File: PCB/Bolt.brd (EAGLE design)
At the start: 160 x 100 mm, 11 parts, among them IC1 D36V28FX, U1 MPU-9250, U2 ESP32-WROOM-32D, U3 TB6612FNG(O,C,8,EL

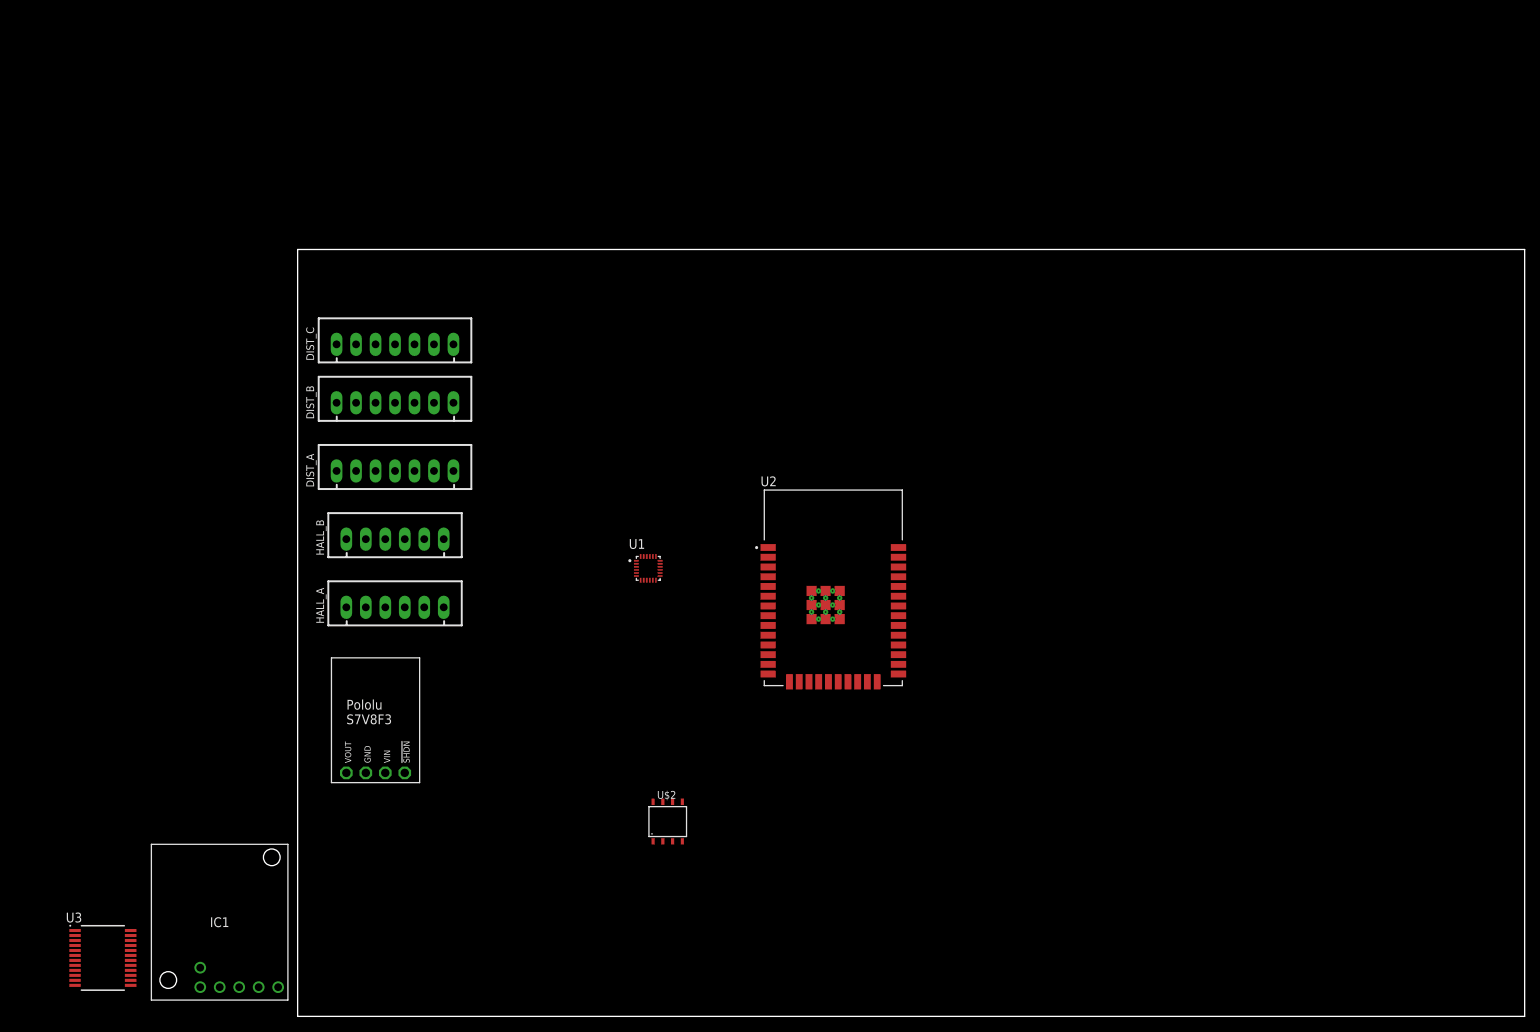
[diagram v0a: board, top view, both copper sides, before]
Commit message: Added UART-USB converter
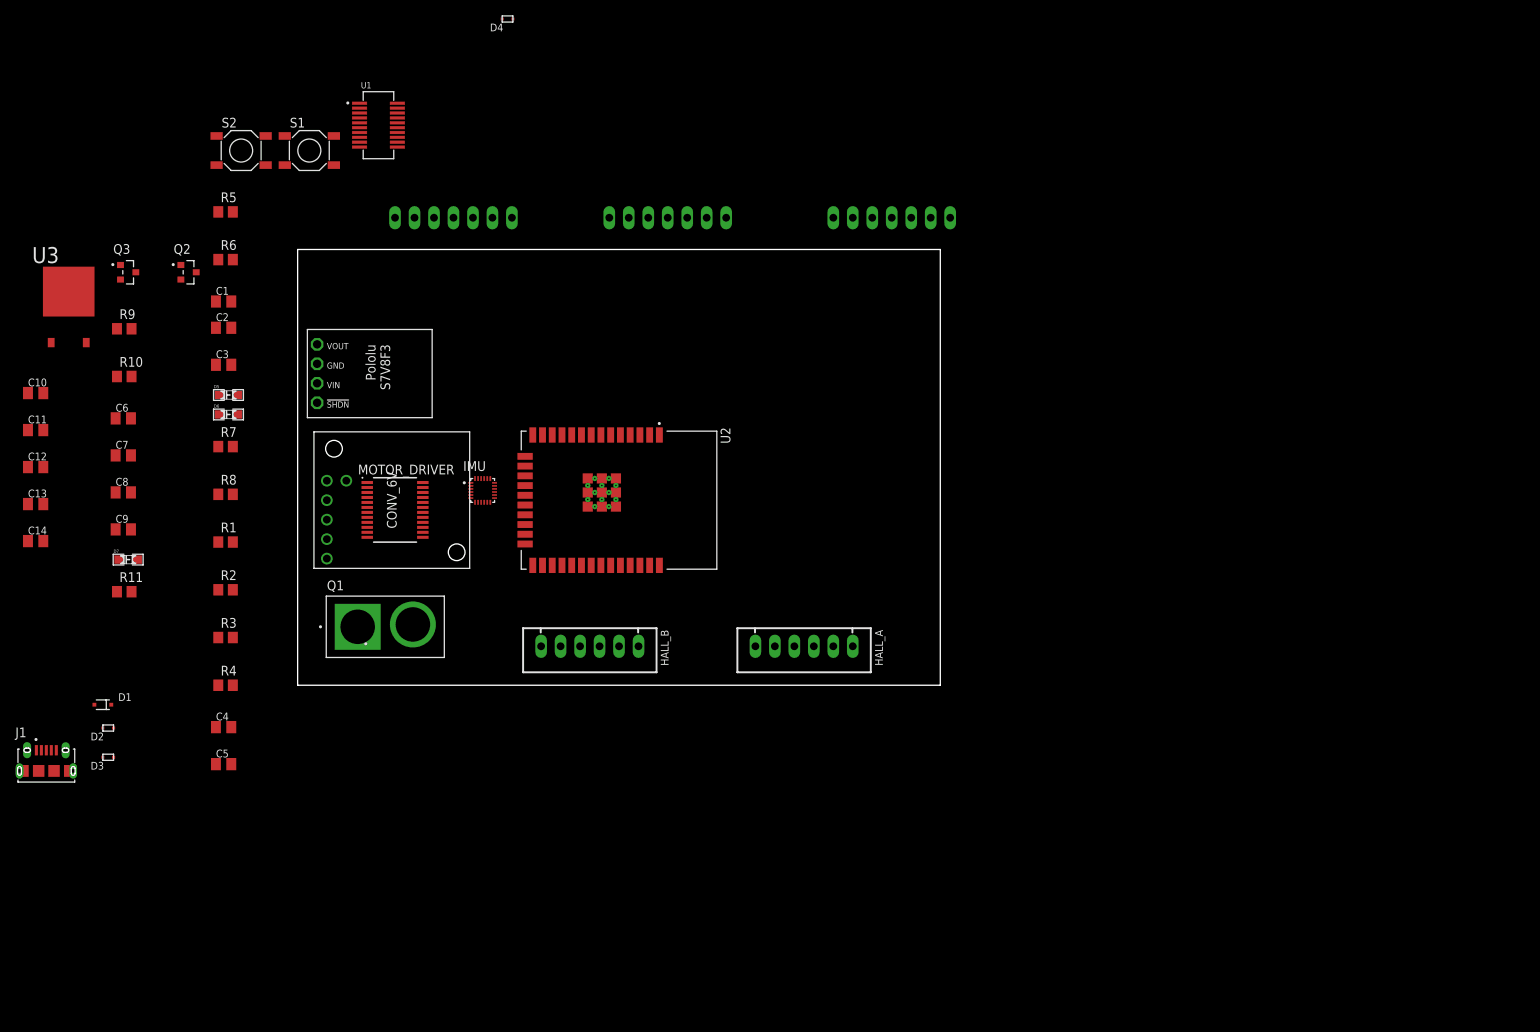
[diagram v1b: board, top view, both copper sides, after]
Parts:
- removed IC1: D36V28FX, D36V28FX:D36V28FX
- removed U$1: S7V8F3, Pololu_S7V8F3:S7V8F3
- removed U$2: TP4056, TP4056:SOT23-8
- added C1, C2: 47pF, rcl:C0805K
- added C10, C13: 1uF, rcl:C0805K
- added C11, C6: 10uF, rcl:C0805K
- added C12, C3, C7, C8: 0.1uF, rcl:C0805K
- added C14: 47uF, rcl:C0805K
- added C4, C5: 1nF, rcl:C0805K
- added C9: 22uF, rcl:C0805K
- added CONV_3V3: S7V8F3, Pololu_S7V8F3:S7V8F3
- added CONV_6V: D36V28FX, D36V28FX:D36V28FX
- added D1: BAT760,115, BAT760_115:SOD323(F)
- added D2, D3, D4: ESD5B5.0ST1G, ESD5B5.0ST1G:SOD-523
- added D5, D6: (no value), leds:0805.LED
- added D7: 3.3V, leds:0805.LED
- added IMU: MPU-9250, MPU-9250:QFN40P300X300X105-24N
- added J1: 10118194-0001LF, 10118194-0001LF:AMPHENOL_10118194-0001LF
- added MOTOR_DRIVER: TB6612FNG(O,C,8,EL, TB6612FNG_O_C_8_EL:SOP65P760X160-24N
- added Q1: XT60_YELLOW, XT60_YELLOW:AMASS_XT60PB-M
- added Q2, Q3: MMSS8050-H-TP, MMSS8050-H-TP:TRANS_MMSS8050-H-TP
- added R1, R2: 220R, rcl:R0805
- added R10, R3, R4, R7, R8, R9: 10K, rcl:R0805
- added R11: 1K, rcl:R0805
- added R5, R6: 27R, rcl:R0805
- added S1, S2: PTS525SM08, pts525_20:SM08
- U1: value MPU-9250 -> FT231XS-R; device MPU-9250:QFN40P300X300X105-24N -> FT231XS-R:SOP63P599X175-20N
- U3: value TB6612FNG(O,C,8,EL -> LM1117DT-3.3/NOPB; device TB6612FNG_O_C_8_EL:SOP65P760X160-24N -> LM1117DT-3.3_NOPB:TO228P970X238-3N
- moved U3 86.9 mm to (-29.8, 94.4)
- moved DIST_B 69.1 mm to (77.5, 104.1), flipped to the bottom
- moved U1 67.7 mm to (10.5, 116.2)
- moved HALL_A 53.6 mm to (66.0, 48.3), turned to 180 degrees
- moved DIST_A 48.5 mm to (48.3, 104.1), flipped to the bottom
- moved U2 30.2 mm to (41.9, 67.3), turned to 270 degrees
- moved HALL_B 29.0 mm to (38.1, 48.3), turned to 180 degrees
- moved DIST_C 18.2 mm to (20.3, 104.1), flipped to the bottom
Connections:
- net N$73 renamed CTS
- removed net VM1: U3.24
- removed net VM2: U3.13
- removed net VM3: U3.14
- new net 6V: CONV_6V.6
- new net DTR: Q2.2, R9.2, U1.1
- new net EN: C5.1, Q3.3, R1.1, R4.2, U2.3
- new net EXT_5V: C10.1, C11.1, D1.1, U1.15, U3.3
- new net GND: C1.2, C10.2, C11.2, C12.2, C13.2, C14.2, C2.2, C3.2, C4.2, C5.2, C6.2, C7.2, C8.2, C9.2, CONV_3V3.GND, CONV_6V.4, CONV_6V.5, D2.P$2, D3.P$2, D4.P$2, J1.1, J1.S1, J1.S2, J1.S3, J1.S4, J1.S5, J1.S6, Q1.2, R11.1, S1.3, S2.3, U1.16, U1.6, U2.1, U2.15, U2.38, U2.39_1, U2.39_10, U2.39_11, U2.39_12, U2.39_13, U2.39_14, U2.39_15, U2.39_16, U2.39_17, U2.39_18, U2.39_19, U2.39_2, U2.39_20, U2.39_21, U2.39_3, U2.39_4, U2.39_5, U2.39_6, U2.39_7, U2.39_8, U2.39_9, U3.1
- new net IO0: C4.1, Q2.3, R2.1, R3.2, U2.25
- new net N$100: MOTOR_DRIVER.2
- new net N$101: MOTOR_DRIVER.5
- new net N$102: MOTOR_DRIVER.6
- new net N$103: MOTOR_DRIVER.1
- new net N$104: MOTOR_DRIVER.24
- new net N$105: MOTOR_DRIVER.13
- new net N$106: MOTOR_DRIVER.14
- new net N$107: MOTOR_DRIVER.20
- new net N$110: CONV_3V3.!SHDN
- new net N$112: CONV_6V.1
- new net N$113: CONV_6V.2
- new net N$122: U1.5
- new net N$124: Q3.1, R9.1
- new net N$126: D5.P$2, U1.17
- new net N$127: D6.P$2, U1.10
- new net N$129: D6.P$1, R8.2
- new net N$73: IMU.9
- new net N$74: IMU.7
- new net N$80: IMU.8
- new net N$84: MOTOR_DRIVER.19
- new net N$85: MOTOR_DRIVER.23
- new net N$86: MOTOR_DRIVER.15
- new net N$87: MOTOR_DRIVER.21
- new net N$88: MOTOR_DRIVER.22
- new net N$89: MOTOR_DRIVER.17
- new net N$90: MOTOR_DRIVER.16
- new net N$91: MOTOR_DRIVER.4
- new net N$92: MOTOR_DRIVER.3
- new net N$93: MOTOR_DRIVER.18
- new net N$94: MOTOR_DRIVER.9
- new net N$95: MOTOR_DRIVER.10
- new net N$96: MOTOR_DRIVER.12
- new net N$97: MOTOR_DRIVER.7
- new net N$98: MOTOR_DRIVER.8
- new net N$99: MOTOR_DRIVER.11
- new net RTS: Q2.1, Q3.2, R10.1, R10.2, U1.2
- new net RXD0: U1.20, U2.34
- new net TXD0: U1.4, U2.35
- new net USB_5V: C6.1, C7.1, D1.2, D4.P$1, J1.5
- new net USB_DM: C2.1, D2.P$1, J1.4, R6.1
- new net USB_DP: C1.1, D3.P$1, J1.3, R5.1
- new net V_BAT: CONV_3V3.VIN, CONV_6V.3, Q1.1
- net N$28: now also D7.P$2, R11.2; no longer U2.2
- net N$35: now also D5.P$1, R7.2; no longer U2.25
- net N$55: now also R5.2, U1.11; no longer U2.3
- net N$56: now also R6.2, U1.12; no longer U2.1, U2.15, U2.38, U2.39_1, U2.39_10, U2.39_11, U2.39_12, U2.39_13, U2.39_14, U2.39_15, U2.39_16, U2.39_17, U2.39_18, U2.39_19, U2.39_2, U2.39_20, U2.39_21, U2.39_3, U2.39_4, U2.39_5, U2.39_6, U2.39_7, U2.39_8, U2.39_9
- net N$61: now also R2.2, S1.1; no longer U2.35
- net N$62: now also R1.2, S2.1; no longer U2.34
- net N$69: now also IMU.11; no longer U1.11
- net N$70: now also IMU.22; no longer U1.22
- net N$71: now also IMU.23; no longer U1.23
- net N$72: now also IMU.24; no longer U1.24
- net N$75: now also IMU.21; no longer U1.21
- net N$76: now also IMU.1; no longer U1.1
- net N$77: now also IMU.19; no longer U1.19
- net N$78: now also IMU.20; no longer U1.20
- net N$79: now also IMU.13; no longer U1.13
- net N$81: now also IMU.12; no longer U1.12
- net N$82: now also IMU.10; no longer U1.10
- net N$83: now also IMU.18; no longer U1.18
- net VCC: now also C12.1, C13.1, C14.1, C3.1, C8.1, C9.1, CONV_3V3.VOUT, D7.P$1, R3.1, R4.1, R7.1, R8.1, U1.13, U1.14, U1.3, U2.2, U3.2; no longer U3.20
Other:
- board size 160 x 100 mm -> 83.8 x 56.8 mm

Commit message: Schematic completed
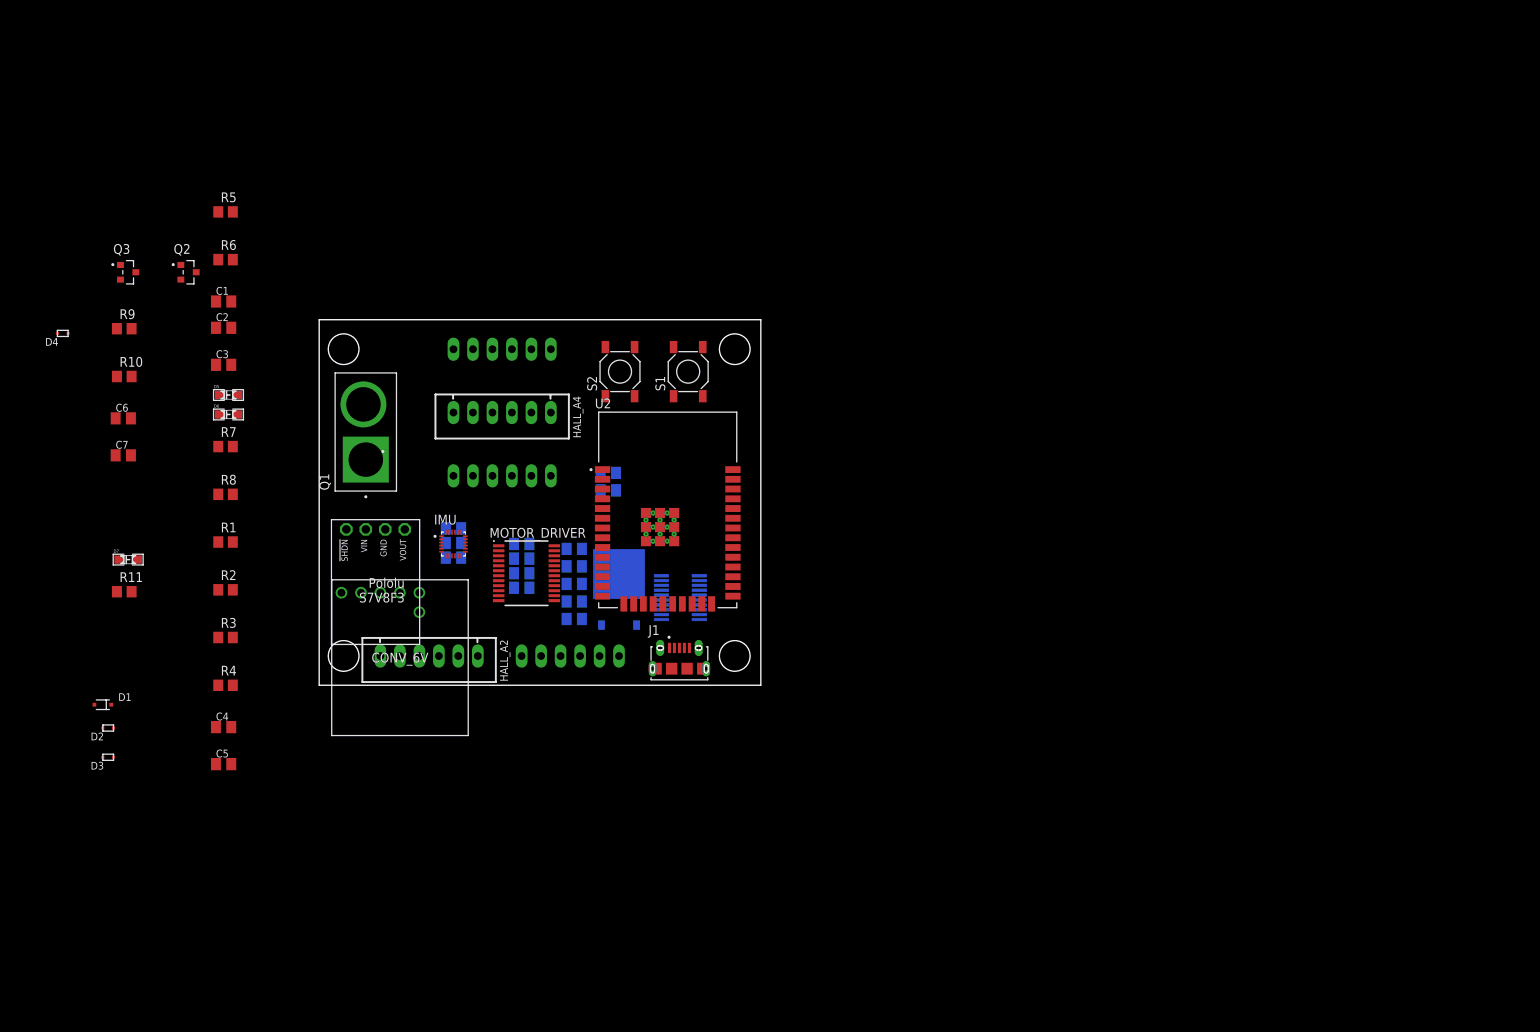
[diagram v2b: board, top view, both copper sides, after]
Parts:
- removed DIST_A, DIST_B, DIST_C: JST-XH-07-PIN-LONG-PAD, Rembrandt Electronics - JST XH Connectors v1-0:JST-XH-07-PACKAGE-LONG-PAD
- removed HALL_B: JST-XH-06-PIN-LONG-PAD, Rembrandt Electronics - JST XH Connectors v1-0:JST-XH-06-PACKAGE-LONG-PAD
- added C15, C17, C19, C20: 0.1uF, rcl:C0805K
- added C16, C18: 10uF, rcl:C0805K
- added C21: 10nF, rcl:C0805K
- added HALL_A1, HALL_A2, HALL_A3, HALL_A4: JST-XH-06-PIN-LONG-PAD, Rembrandt Electronics - JST XH Connectors v1-0:JST-XH-06-PACKAGE-LONG-PAD
- moved J1 83.6 mm to (49.8, 45.3)
- moved U3 80.7 mm to (41.9, 57.5), flipped to the bottom
- moved C10 73.1 mm to (36.1, 61.0), flipped to the bottom
- moved U1 73.1 mm to (49.9, 54.6), flipped to the bottom, turned to 180 degrees
- moved C11 72.4 mm to (36.1, 58.7), flipped to the bottom
- moved C12 71.9 mm to (36.1, 56.4), flipped to the bottom
- moved C13 71.4 mm to (36.1, 54.1), flipped to the bottom
- moved D4 71.0 mm to (-31.3, 89.6)
- moved C14 71.0 mm to (36.1, 51.8), flipped to the bottom
- moved C9 63.4 mm to (40.5, 68.6), flipped to the bottom
- moved C8 63.3 mm to (40.5, 70.9), flipped to the bottom
- moved S1 57.2 mm to (50.9, 84.1), turned to 90 degrees
- moved S2 57.2 mm to (42.0, 84.1), turned to 90 degrees
- moved HALL_A 30.5 mm to (35.6, 47.0), flipped to the bottom
- moved Q1 25.5 mm to (8.89, 76.2), turned to 90 degrees
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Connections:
- net N$25 renamed HALL_1_A
- net N$69 renamed IMU_FSYNC
- net N$70 renamed IMU_CS
- net N$71 renamed IMU_CLK
- net N$72 renamed IMU_SDI
- net N$73 renamed IMU_SDO
- net N$81 renamed IMU_INT
- net N$84 renamed M_DRV_STBY
- net N$85 renamed M_DRV_PWMA
- net N$86 renamed M_DRV_PWMB
- net N$87 renamed M_DRV_AIN1
- net N$88 renamed M_DRV_AIN2
- net N$89 renamed M_DRV_BIN1
- net N$90 renamed M_DRV_BIN2
- removed net N$1: DIST_A.1
- removed net N$10: DIST_B.3
- removed net N$100: MOTOR_DRIVER.2
- removed net N$101: MOTOR_DRIVER.5
- removed net N$102: MOTOR_DRIVER.6
- removed net N$103: MOTOR_DRIVER.1
- removed net N$104: MOTOR_DRIVER.24
- removed net N$105: MOTOR_DRIVER.13
- removed net N$106: MOTOR_DRIVER.14
- removed net N$107: MOTOR_DRIVER.20
- removed net N$11: DIST_B.4
- removed net N$12: DIST_B.5
- removed net N$13: DIST_B.6
- removed net N$14: DIST_B.7
- removed net N$15: DIST_C.1
- removed net N$16: DIST_C.2
- removed net N$17: DIST_C.3
- removed net N$18: DIST_C.4
- removed net N$19: DIST_C.5
- removed net N$2: DIST_A.2
- removed net N$20: DIST_C.6
- removed net N$21: DIST_C.7
- removed net N$22: HALL_A.1
- removed net N$23: HALL_A.2
- removed net N$24: HALL_A.3
- removed net N$26: HALL_A.5
- removed net N$27: HALL_A.6
- removed net N$29: HALL_B.1
- removed net N$3: DIST_A.3
- removed net N$30: HALL_B.2
- removed net N$31: HALL_B.3
- removed net N$32: HALL_B.4
- removed net N$33: HALL_B.5
- removed net N$34: HALL_B.6
- removed net N$4: DIST_A.4
- removed net N$42: U2.23
- removed net N$47: U2.33
- removed net N$48: U2.36
- removed net N$5: DIST_A.5
- removed net N$6: DIST_A.6
- removed net N$7: DIST_A.7
- removed net N$74: IMU.7
- removed net N$75: IMU.21
- removed net N$76: IMU.1
- removed net N$78: IMU.20
- removed net N$79: IMU.13
- removed net N$8: DIST_B.1
- removed net N$80: IMU.8
- removed net N$82: IMU.10
- removed net N$83: IMU.18
- removed net N$9: DIST_B.2
- removed net N$91: MOTOR_DRIVER.4
- removed net N$92: MOTOR_DRIVER.3
- removed net N$93: MOTOR_DRIVER.18
- removed net N$94: MOTOR_DRIVER.9
- removed net N$95: MOTOR_DRIVER.10
- removed net N$96: MOTOR_DRIVER.12
- removed net N$97: MOTOR_DRIVER.7
- removed net N$98: MOTOR_DRIVER.8
- removed net N$99: MOTOR_DRIVER.11
- new net DIST_GPIO1_A: HALL_A1.6
- new net DIST_GPIO1_B: HALL_A3.6
- new net DIST_GPIO1_C: HALL_A4.6
- new net DIST_XSHUT_A: HALL_A1.5
- new net DIST_XSHUT_B: HALL_A3.5
- new net DIST_XSHUT_C: HALL_A4.5
- new net HALL_1_B: HALL_A2.4
- new net HALL_2_A: HALL_A.5, U2.23
- new net HALL_2_B: HALL_A2.5
- new net I2C_SCL: HALL_A1.4, HALL_A3.4, HALL_A4.4, U2.36
- new net I2C_SDA: HALL_A1.3, HALL_A3.3, HALL_A4.3, U2.33
- new net M1_A: HALL_A.1, MOTOR_DRIVER.1, MOTOR_DRIVER.2
- new net M1_B: HALL_A2.1, MOTOR_DRIVER.11, MOTOR_DRIVER.12
- new net M2_A: HALL_A.2, MOTOR_DRIVER.5, MOTOR_DRIVER.6
- new net M2_B: HALL_A2.2, MOTOR_DRIVER.7, MOTOR_DRIVER.8
- new net REGOUT: C20.1, IMU.10
- net 6V: now also C17.1, C18.1, MOTOR_DRIVER.13, MOTOR_DRIVER.14, MOTOR_DRIVER.24
- net GND: now also C15.2, C16.2, C17.2, C18.2, C19.2, C20.2, C21.2, HALL_A.6, HALL_A1.2, HALL_A2.6, HALL_A3.2, HALL_A4.2, IMU.18, IMU.20, MOTOR_DRIVER.10, MOTOR_DRIVER.18, MOTOR_DRIVER.3, MOTOR_DRIVER.4, MOTOR_DRIVER.9
- net VCC: now also C15.1, C16.1, C19.1, C21.1, HALL_A.3, HALL_A1.1, HALL_A2.3, HALL_A3.1, HALL_A4.1, IMU.1, IMU.13, IMU.8, MOTOR_DRIVER.20
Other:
- board size 83.8 x 56.8 mm -> 57.6 x 47.7 mm

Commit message: Board - work in progress
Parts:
- moved D4 88.2 mm to (48.4, 51.9), turned to 90 degrees
- moved C6 80.5 mm to (53.6, 52.5), flipped to the bottom, turned to 180 degrees
- moved R11 79.5 mm to (56.9, 54.8), flipped to the bottom, turned to 180 degrees
- moved D1 79.2 mm to (52.9, 53.0), turned to 90 degrees
- moved D7 79.0 mm to (56.8, 54.8)
- moved C5 78.6 mm to (54.1, 78.9), flipped to the bottom, turned to 270 degrees
- moved D3 77.4 mm to (49.9, 51.9), turned to 90 degrees
- moved R5 77.2 mm to (49.6, 55.1), flipped to the bottom
- moved C7 77.1 mm to (50.2, 48.1), flipped to the bottom
- moved R4 76.6 mm to (58.4, 78.9), flipped to the bottom, turned to 90 degrees
- moved R10 73.7 mm to (49.1, 66.4), flipped to the bottom, turned to 270 degrees
- moved D2 73.5 mm to (46.8, 51.9), turned to 90 degrees
- moved R6 73.5 mm to (49.8, 55.2)
- moved R9 72.9 mm to (46.5, 66.5), flipped to the bottom, turned to 270 degrees
- moved C4 71.5 mm to (54.0, 70.3), flipped to the bottom, turned to 270 degrees
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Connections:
- removed net N$50: U2.10
- removed net N$51: U2.11
- removed net N$53: U2.8
- removed net N$54: U2.9
- removed net N$57: U2.4
- removed net N$58: U2.5
- removed net N$59: U2.6
- removed net N$60: U2.7
- new net L: U2.33
- new net LL: U2.36
- new net N$1: Q2.1, R10.2
- net DIST_GPIO1_A: now also U2.9
- net DIST_GPIO1_B: now also U2.4
- net DIST_GPIO1_C: now also U2.7
- net DIST_XSHUT_A: now also U2.8
- net DIST_XSHUT_B: now also U2.5
- net DIST_XSHUT_C: now also U2.6
- net I2C_SCL: now also U2.10; no longer U2.36
- net I2C_SDA: now also U2.11; no longer U2.33
- net RTS: no longer Q2.1, R10.2
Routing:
- net V_BAT: track 0.00 -> 36.0 mm
- net GND: track 0.00 -> 35.8 mm, vias 0 -> 27
- net I2C_SDA: track 0.00 -> 26.6 mm, vias 0 -> 2
- net EN: track 0.00 -> 26.0 mm, vias 0 -> 1
- net I2C_SCL: track 0.00 -> 24.9 mm
- net M2_B: track 0.00 -> 20.7 mm
- net VCC: track 0.00 -> 17.4 mm, vias 0 -> 11
- net M1_B: track 0.00 -> 16.8 mm
- net 6V: track 0.00 -> 16.2 mm, vias 0 -> 1
- net DIST_XSHUT_A: track 0.00 -> 11.8 mm, vias 0 -> 1
- net M2_A: track 0.00 -> 9.91 mm
- net DIST_XSHUT_B: track 0.00 -> 9.38 mm
- net DIST_GPIO1_A: track 0.00 -> 9.27 mm, vias 0 -> 1
- net DIST_XSHUT_C: track 0.00 -> 9.14 mm
- net M1_A: track 0.00 -> 8.27 mm
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- added copper zone on layer 15, net GND
- added copper zone on layer 2, net VCC
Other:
- board size 57.6 x 47.7 mm -> 57.6 x 42.9 mm
